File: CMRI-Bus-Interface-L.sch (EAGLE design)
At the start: 23 parts, among them CON1 0.100, CON2 0.100, J1 0.100, M1 MOUNTINGHOLE, M2 MOUNTINGHOLE, M3 MOUNTINGHOLE, M4 MOUNTINGHOLE, U1 MAX3465CSD, U2 NE555

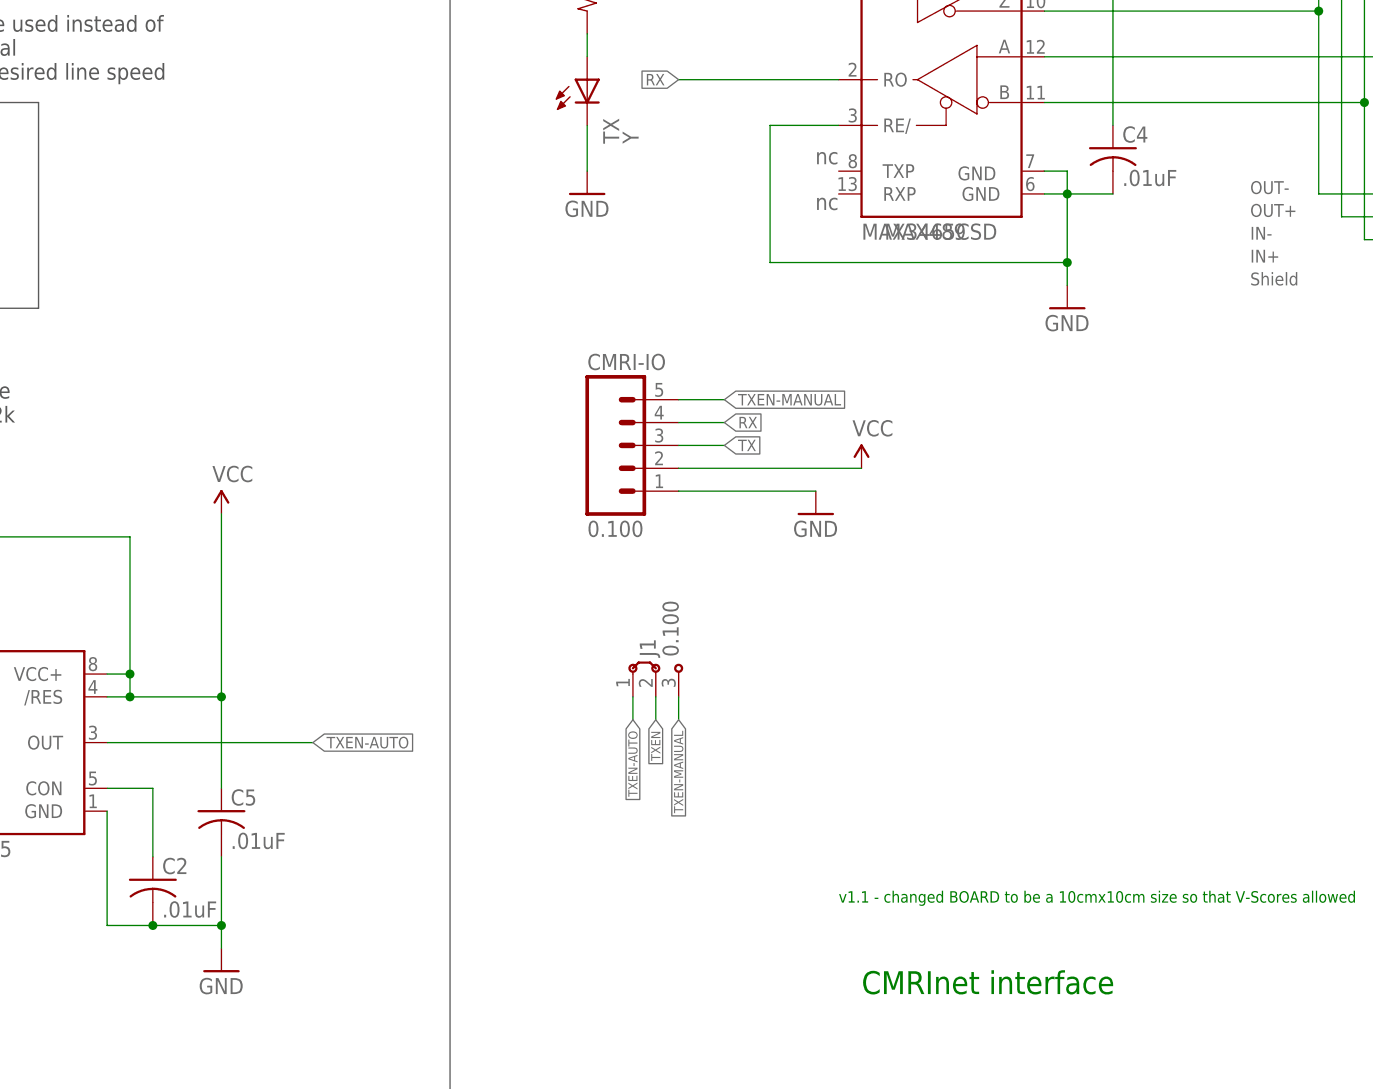
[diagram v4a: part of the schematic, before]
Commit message: normalized values
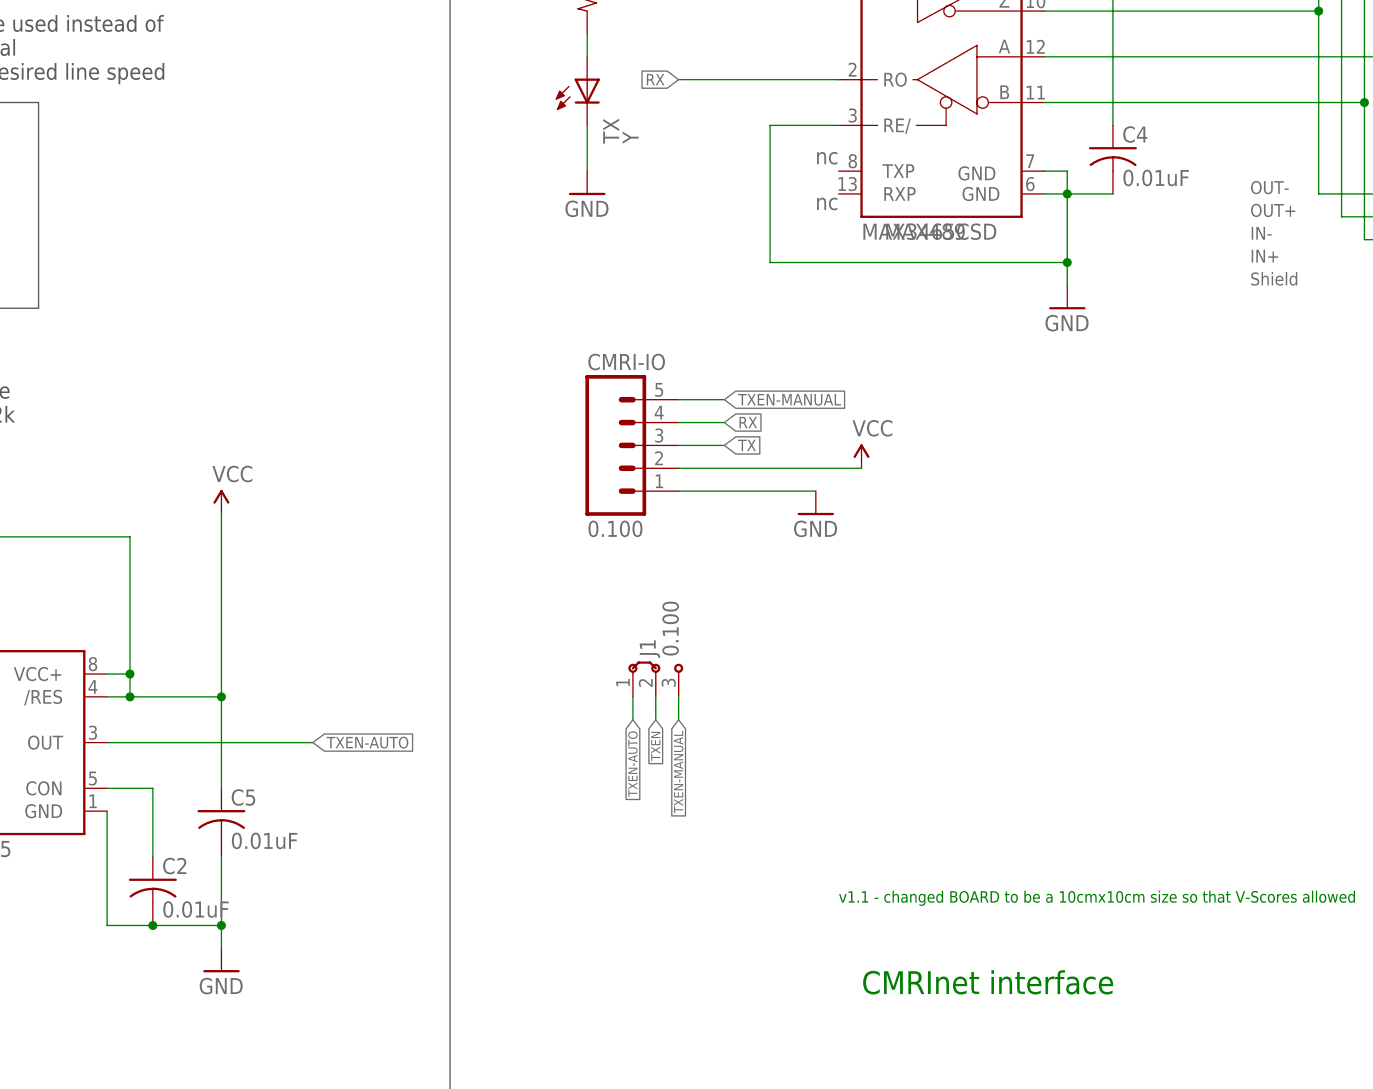
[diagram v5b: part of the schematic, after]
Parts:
- C2, C4, C5: value .01uF -> 0.01uF
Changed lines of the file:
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@@
 <part name="U1" library="SPCoast" deviceset="MAX346*" device="SD" technology="5C" value="MAX3465CSD"/>
 <part name="C1" library="SPCoast" deviceset="CAP*" device="0603" value="0.1uF"/>
-<part name="C2" library="SPCoast" deviceset="CAP*" device="0603" value=".01uF"/>
+<part name="C2" library="SPCoast" deviceset="CAP*" device="0603" value="0.01uF"/>
 <part name="R1" library="SPCoast" deviceset="R*" device="PTH04" value="12k"/>
 <part name="D1" library="SPCoast" deviceset="DIODE-BAV199" device="" value="BAV199"/>
@@
 <part name="P+2" library="SparkFun" deviceset="VCC" device=""/>
 <part name="GND3" library="SparkFun" deviceset="GND" device=""/>
-<part name="C4" library="SPCoast" deviceset="CAP*" device="0603" value=".01uF"/>
-<part name="C5" library="SPCoast" deviceset="CAP*" device="0603" value=".01uF"/>
+<part name="C4" library="SPCoast" deviceset="CAP*" device="0603" value="0.01uF"/>
+<part name="C5" library="SPCoast" deviceset="CAP*" device="0603" value="0.01uF"/>
 <part name="R2" library="SPCoast" deviceset="R*" device="0805-RES" value="470"/>
 <part name="GND9" library="SparkFun" deviceset="GND" device=""/>
